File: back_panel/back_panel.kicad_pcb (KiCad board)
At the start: 2 copper layers, 68.8 x 19.8 mm, 0 parts

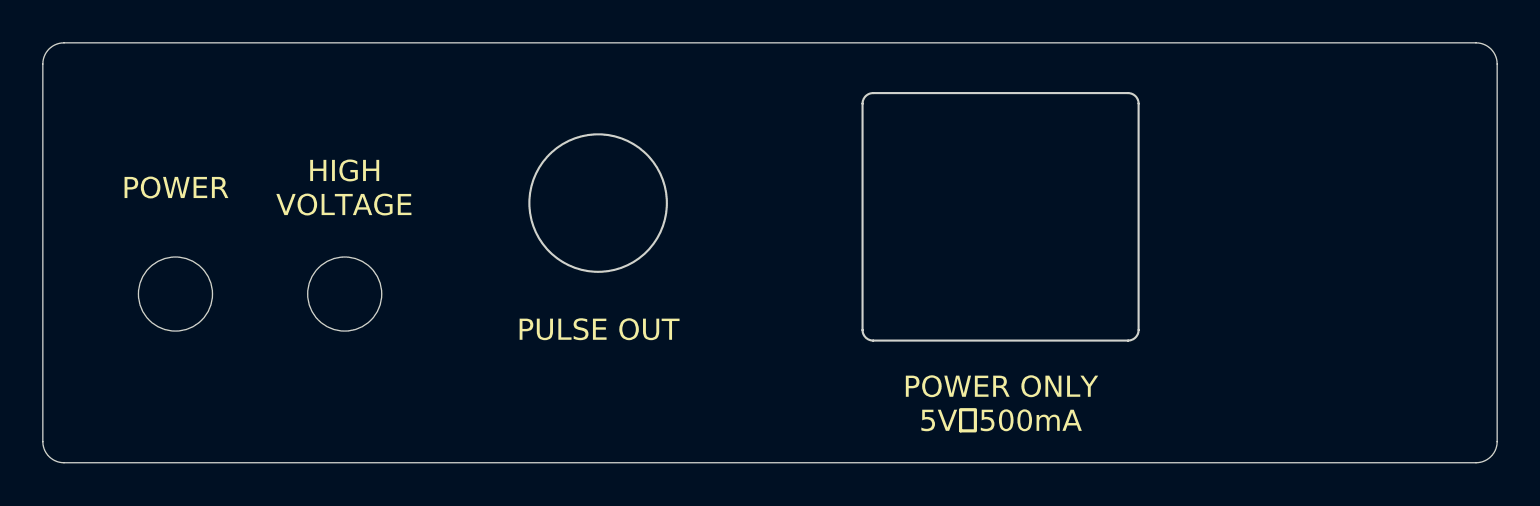
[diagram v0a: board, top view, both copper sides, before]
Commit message: Increase LED cutout radius, add back panel
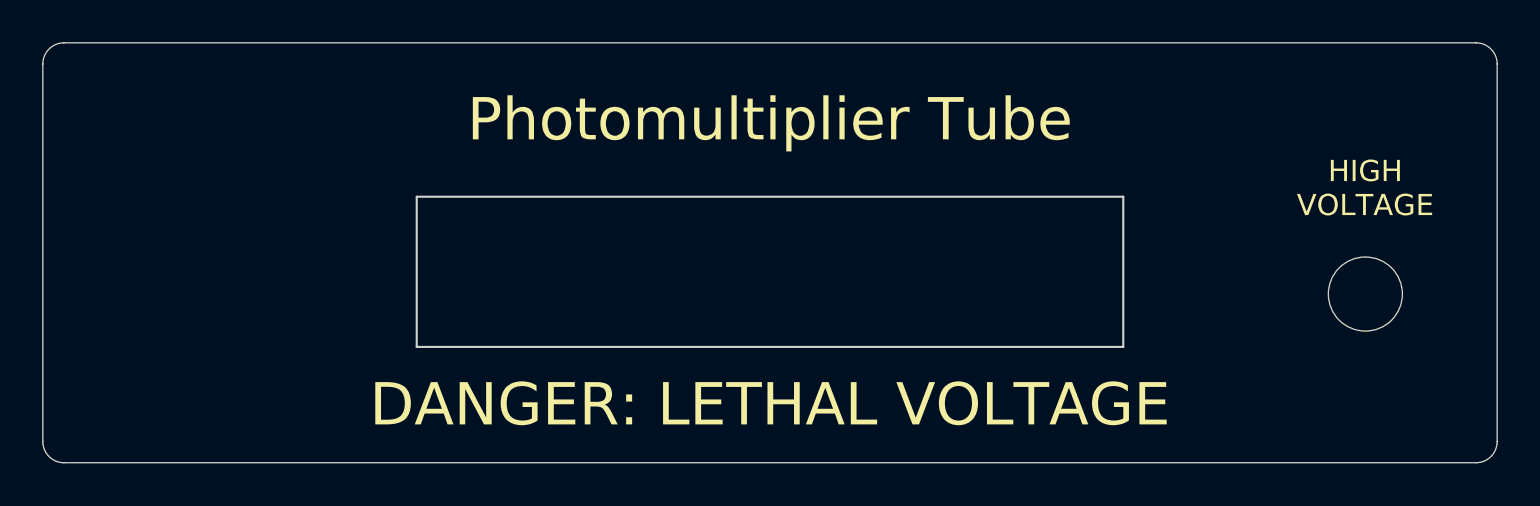
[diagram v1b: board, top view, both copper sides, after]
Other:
- outline, holes or cut-outs redrawn
- board text added: "DANGER: LETHAL VOLTAGE"
- board text added: "Photomultiplier Tube"
- board text removed: "POWER"
- board text removed: "POWER ONLY 5V⎓500mA"
- board text removed: "PULSE OUT"
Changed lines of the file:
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@@
 	(net 0 "")
 	(gr_line
-		(start 110.9 104.15)
-		(end 110.9 92.45)
-		(stroke
-			(width 0.1)
+		(start 100 97.35)
+		(end 100 90.075)
+		(stroke
+			(width 0.05)
+			(type default)
+		)
+		(layer "Dwgs.User")
+	)
+	(gr_line
+		(start 100 104.45)
+		(end 100 109.925)
+		(stroke
+			(width 0.05)
 			(type default)
 		)
@@
 	)
 	(gr_rect
-		(start 104.375 92.45)
-		(end 117.425 104.15)
+		(start 83.8 97.85)
+		(end 116.2 103.95)
 		(locked yes)
 		(stroke
@@
 	)
 	(gr_line
-		(start 116.925 104.15)
-		(end 104.875 104.15)
-		(locked yes)
-		(stroke
-			(width 0.1)
-			(type default)
-		)
-		(layer "Edge.Cuts")
-	)
-	(gr_line
 		(start 66.625 90.075)
 		(end 133.375 90.075)
@@
 			(type default)
 		)
-		(layer "Edge.Cuts")
-	)
-	(gr_circle
-		(center 79.895 101.95)
-		(end 81.645 101.95)
-		(locked yes)
-		(stroke
-			(width 0.05)
-			(type default)
-		)
-		(fill none)
 		(layer "Edge.Cuts")
 	)
@@
 		(layer "Edge.Cuts")
 	)
-	(gr_circle
-		(center 71.895 101.95)
-		(end 73.645 101.95)
-		(locked yes)
-		(stroke
-			(width 0.05)
-			(type default)
-		)
-		(fill none)
-		(layer "Edge.Cuts")
-	)
 	(gr_arc
 		(start 65.625 91.075)
@@
 		(layer "Edge.Cuts")
 	)
-	(gr_line
-		(start 117.425 92.95)
-		(end 117.425 103.65)
-		(locked yes)
+	(gr_rect
+		(start 83.3 97.35)
+		(end 116.7 104.45)
 		(stroke
 			(width 0.1)
 			(type default)
 		)
-		(layer "Edge.Cuts")
-	)
-	(gr_arc
-		(start 117.425 103.65)
-		(mid 117.278553 104.003553)
-		(end 116.925 104.15)
-		(locked yes)
-		(stroke
-			(width 0.1)
-			(type default)
-		)
-		(layer "Edge.Cuts")
-	)
-	(gr_arc
-		(start 116.925 92.45)
-		(mid 117.278553 92.596447)
-		(end 117.425 92.95)
-		(locked yes)
-		(stroke
-			(width 0.1)
-			(type default)
-		)
+		(fill none)
 		(layer "Edge.Cuts")
 	)
@@
 		(layer "Edge.Cuts")
 	)
-	(gr_line
-		(start 104.875 92.45)
-		(end 116.925 92.45)
-		(locked yes)
-		(stroke
-			(width 0.1)
-			(type default)
-		)
-		(layer "Edge.Cuts")
-	)
-	(gr_arc
-		(start 104.875 104.15)
-		(mid 104.521447 104.003553)
-		(end 104.375 103.65)
-		(locked yes)
-		(stroke
-			(width 0.1)
-			(type default)
-		)
-		(layer "Edge.Cuts")
-	)
 	(gr_circle
-		(center 91.875 97.65)
-		(end 95.125 97.65)
-		(locked yes)
-		(stroke
-			(width 0.1)
+		(center 128.145 101.95)
+		(end 129.895 101.95)
+		(locked yes)
+		(stroke
+			(width 0.05)
 			(type default)
 		)
@@
 	)
 	(gr_line
-		(start 104.375 103.65)
-		(end 104.375 92.95)
-		(locked yes)
-		(stroke
-			(width 0.1)
-			(type default)
-		)
-		(layer "Edge.Cuts")
-	)
-	(gr_line
 		(start 65.625 108.925)
 		(end 65.625 91.075)
@@
 		(layer "Edge.Cuts")
 	)
-	(gr_arc
-		(start 104.375 92.95)
-		(mid 104.521447 92.596447)
-		(end 104.875 92.45)
-		(locked yes)
-		(stroke
-			(width 0.1)
-			(type default)
-		)
-		(layer "Edge.Cuts")
-	)
-	(gr_text "POWER ONLY\n5V⎓500mA"
-		(at 110.9 107.15 0)
+	(gr_text "Photomultiplier Tube"
+		(at 100 93.7125 0)
 		(layer "F.SilkS")
 		(effects
 			(font
-				(size 1 1)
-				(thickness 0.15)
-			)
-		)
-	)
-	(gr_text "HIGH\nVOLTAGE"
-		(at 79.895 96.95 0)
+				(size 2 2)
+				(thickness 0.3)
+			)
+		)
+	)
+	(gr_text "DANGER: LETHAL VOLTAGE"
+		(at 100 107.1875 0)
 		(layer "F.SilkS")
 		(effects
 			(font
-				(size 1 1)
-				(thickness 0.15)
-			)
-		)
-	)
-	(gr_text "PULSE OUT"
-		(at 91.875 103.65 0)
-		(layer "F.SilkS")
-		(effects
-			(font
-				(size 1 1)
-				(thickness 0.15)
-			)
-		)
-	)
-	(gr_text "POWER"
-		(at 71.895 96.95 0)
+				(size 2 2)
+				(thickness 0.3)
+			)
+		)
+	)
+	(gr_text "HIGH\nVOLTAGE"
+		(at 128.145 96.95 0)
 		(layer "F.SilkS")
 		(effects
@@
 			(layer "Dwgs.User")
 			(effects
-				(font
-					(size 1 1)
-					(thickness 0.15)
-				)
-			)
-		)
-		(format
-			(prefix "")
-			(suffix "")
-			(units 3)
-			(units_format 1)
-			(precision 4)
-		)
-		(style
-			(thickness 0.1)
-			(arrow_length 1.27)
-			(text_position_mode 0)
-			(extension_height 0.58642)
-			(extension_offset 0.5) keep_text_aligned)
-	)
-	(dimension
-		(type aligned)
-		(layer "Dwgs.User")
-		(pts
-			(xy 79.895 101.95) (xy 71.895 101.95)
-		)
-		(height -4.05)
-		(gr_text "8.0000 mm"
-			(at 75.895 104.85 0)
-			(layer "Dwgs.User")
-			(effects
